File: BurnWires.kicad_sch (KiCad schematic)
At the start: 29 parts, among them Q13 IRLML2803, Q14 SiRA99DP, Q15 IRFTS9342PBF, Q17 IRFTS9342PBF, Q19 IRFTS9342PBF

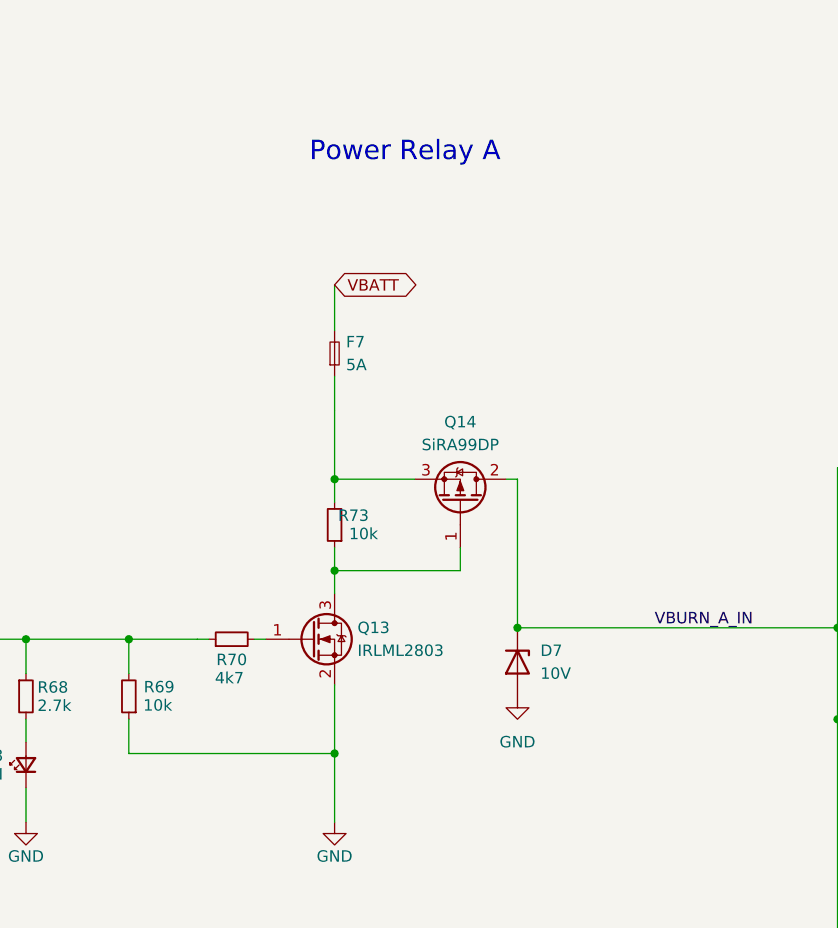
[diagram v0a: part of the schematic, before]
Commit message: Started adding pmos -> relay
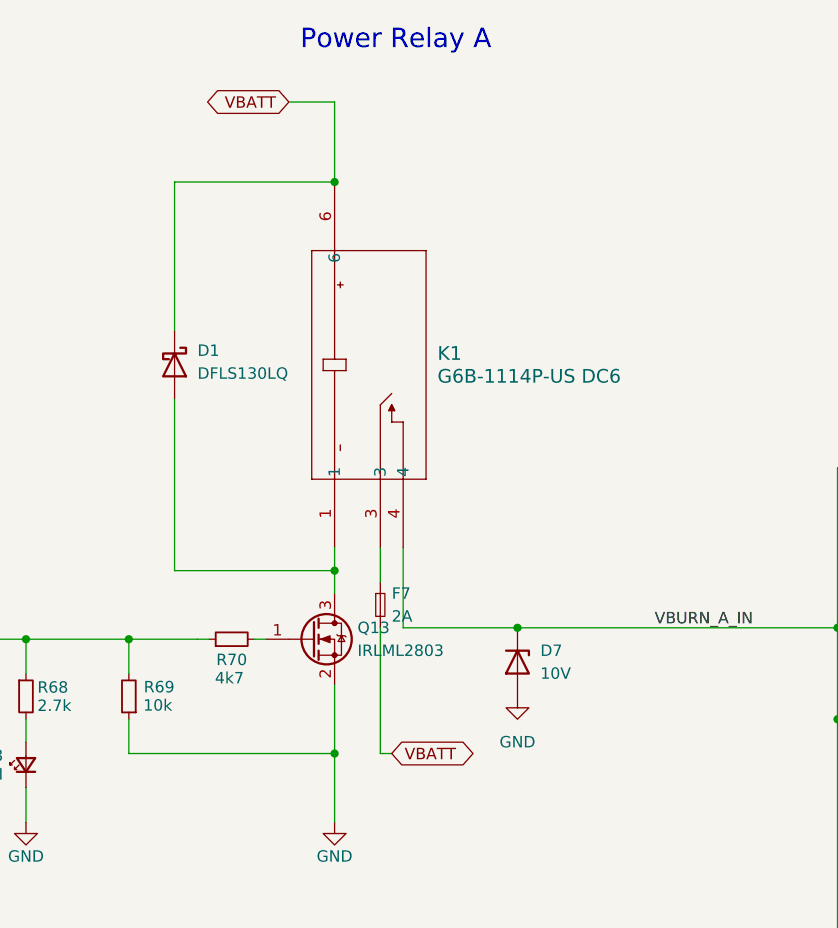
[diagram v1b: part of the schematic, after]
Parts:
- removed Q14: SiRA99DP, Argus-Miscellaneous:PowerPAK SO-8, symbol Argus-IC:Q_PMOS_GDS
- removed R73: 10k, Resistor_SMD:R_0603_1608Metric, symbol Device:R_Small
- added D1: DFLS130LQ, Diode_SMD:D_PowerDI-123, symbol Device:D_Schottky
- added K1: G6B-1114P-US DC6, Argus-Miscellaneous:RELAY_G6B-1114P-US_OMR, symbol Argus-Miscellaneous:G6B-1114P-US_DC6
- F7: value 5A -> 2A
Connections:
- net VBATT: now also D1.1 (K), K1.6
- net VBURN_A_IN: now also K1.4
- net at Q13.3 (D): now also D1.2 (A), K1.1
- net at F7.1: now also K1.3
